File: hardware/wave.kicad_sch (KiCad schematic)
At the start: 62 parts, among them J101 WAGO 2065-100, J102 WAGO 2065-100, J103 Cortex, J104 WAGO 2065-100, J105 WAGO 2065-100, J106 WAGO 2065-100, J107 WAGO 2065-100, SW101 SKSG, SW102 SKSG, U101 ATSAMD51J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

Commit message: Refresh
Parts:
- C101, C102: Manufacturer YAGEO -> TDK; Mouser 603-CC603JRNPO9BN180 -> 810-CGA3E2C0G1H180J; Product CC0603JRNPO9BN180 -> CGA3E2C0G1H180J080AA
- INFO101: value ~ -> (none)
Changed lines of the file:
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@@
 	(title_block
 		(title "V2 wave")
-		(date "2026-02-11")
-		(rev "2026-02-11")
+		(date "2026-03-11")
+		(rev "2026-03-11")
 		(company "Versio Duo")
 		(comment 1 "Power Amplifier")
@@
 			)
 		)
-		(property "Description" "Unpolarized capacitor, small symbol"
+		(property "Description" ""
 			(at 109.22 24.13 0)
 			(effects
@@
 			)
 		)
-		(property "Description" "Push button switch, generic, two pins"
+		(property "Description" "Push button"
 			(at 256.54 30.48 0)
 			(effects
@@
 			)
 		)
-		(property "Description" "Ferrite bead, small symbol"
+		(property "Description" ""
 			(at 85.09 148.59 0)
 			(effects
@@
 			)
 		)
-		(property "Description" "Light emitting diode, small symbol"
+		(property "Description" ""
 			(at 129.54 53.34 0)
 			(effects
@@
 			)
 		)
-		(property "Description" "Resistor, small symbol"
+		(property "Description" ""
 			(at 85.09 170.18 0)
 			(effects
@@
 			)
 		)
-		(property "Description" "Resistor, small symbol"
+		(property "Description" ""
 			(at 21.59 186.69 0)
 			(effects
@@
 			)
 		)
-		(property "Description" "Unpolarized capacitor, small symbol"
+		(property "Description" ""
 			(at 199.39 45.72 0)
 			(effects
@@
 			)
 		)
-		(property "Description" "Unpolarized capacitor, small symbol"
+		(property "Description" ""
 			(at 119.38 24.13 0)
 			(effects
@@
 			)
 		)
-		(property "Description" "Resistor, small symbol"
+		(property "Description" ""
 			(at 35.56 182.88 0)
 			(effects
@@
 			)
 		)
-		(property "Value" "~"
+		(property "Value" ""
 			(at 175.895 170.815 0)
 			(effects
@@
 			)
 		)
-		(property "Description" "Unpolarized capacitor, small symbol"
+		(property "Description" ""
 			(at 173.99 45.72 0)
 			(effects
@@
 			)
 		)
-		(property "Description" "Resistor, small symbol"
+		(property "Description" ""
 			(at 21.59 179.07 0)
 			(effects
@@
 			)
 		)
-		(property "Description" "Two pin crystal, small symbol"
+		(property "Description" ""
 			(at 24.13 43.18 0)
 			(effects
@@
 			)
 		)
-		(property "Description" "Unpolarized capacitor, small symbol"
+		(property "Description" ""
 			(at 26.67 46.99 0)
 			(effects
@@
 			)
 		)
-		(property "Mouser" "603-CC603JRNPO9BN180"
+		(property "Mouser" "810-CGA3E2C0G1H180J"
 			(at 26.67 70.358 0)
 			(effects
@@
 			)
 		)
-		(property "Product" "CC0603JRNPO9BN180"
+		(property "Product" "CGA3E2C0G1H180J080AA"
 			(at 26.67 67.564 0)
 			(effects
@@
 			)
 		)
-		(property "Manufacturer" "YAGEO"
+		(property "Manufacturer" "TDK"
 			(at 26.67 64.77 0)
 			(effects
@@
 			)
 		)
-		(property "Description" "Unpolarized capacitor, small symbol"
+		(property "Description" ""
 			(at 57.15 24.13 0)
 			(effects
@@
 			)
 		)
-		(property "Description" "Unpolarized capacitor, small symbol"
+		(property "Description" ""
 			(at 21.59 46.99 0)
 			(effects
@@
 			)
 		)
-		(property "Mouser" "603-CC603JRNPO9BN180"
+		(property "Mouser" "810-CGA3E2C0G1H180J"
 			(at 21.59 70.358 0)
 			(effects
@@
 			)
 		)
-		(property "Product" "CC0603JRNPO9BN180"
+		(property "Product" "CGA3E2C0G1H180J080AA"
 			(at 21.59 67.564 0)
 			(effects
@@
 			)
 		)
-		(property "Manufacturer" "YAGEO"
+		(property "Manufacturer" "TDK"
 			(at 21.59 64.77 0)
 			(effects
@@
 			)
 		)
-		(property "Description" "Unpolarized capacitor, small symbol"
+		(property "Description" ""
 			(at 45.72 186.69 0)
 			(effects
@@
 			)
 		)
-		(property "Description" "Resistor, small symbol"
+		(property "Description" ""
 			(at 138.43 53.34 0)
 			(effects
@@
 			)
 		)
-		(property "Description" "Resistor, small symbol"
+		(property "Description" ""
 			(at 87.63 170.18 0)
 			(effects
@@
 			)
 		)
-		(property "Description" "Unpolarized capacitor, small symbol"
+		(property "Description" ""
 			(at 99.06 24.13 0)
 			(effects
@@
 			)
 		)
-		(property "Description" "Unpolarized capacitor, small symbol"
+		(property "Description" ""
 			(at 81.28 151.13 0)
 			(effects
@@
 			)
 		)
-		(property "Description" "Unpolarized capacitor, small symbol"
+		(property "Description" ""
 			(at 67.31 151.13 0)
 			(effects
@@
 			)
 		)
-		(property "Description" "Unpolarized capacitor, small symbol"
+		(property "Description" ""
 			(at 78.74 24.13 0)
 			(effects
@@
 			)
 		)
-		(property "Description" "Resistor, small symbol"
+		(property "Description" ""
 			(at 104.14 185.42 0)
 			(effects
@@
 			)
 		)
-		(property "Description" "Push button switch, generic, two pins"
+		(property "Description" "Push button"
 			(at 130.81 40.64 0)
 			(effects
@@
 			)
 		)
-		(property "Description" "Unpolarized capacitor, small symbol"
+		(property "Description" ""
 			(at 88.9 24.13 0)
 			(effects
@@
 			)
 		)
-		(property "Description" "Resistor, small symbol"
+		(property "Description" ""
 			(at 50.8 121.92 0)
 			(effects

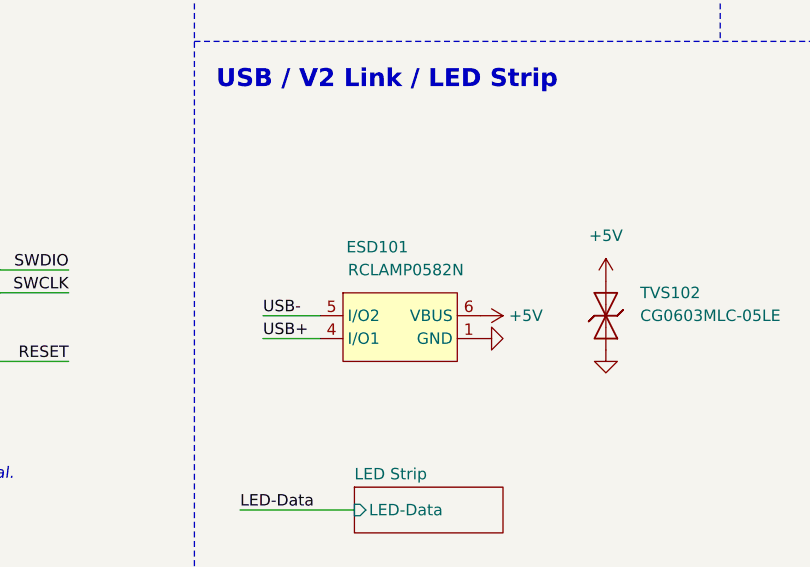
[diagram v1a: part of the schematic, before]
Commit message: Update ESD suppressor
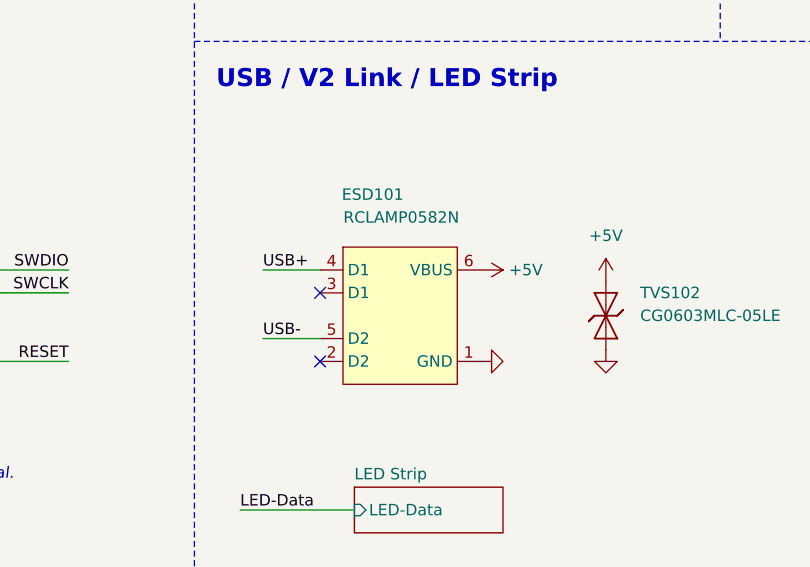
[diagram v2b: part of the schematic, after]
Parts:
- INFO101: value (none) -> ~
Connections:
- no-connect marks 27 -> 29
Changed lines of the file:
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@@
 	(title_block
 		(title "V2 wave")
-		(date "2026-03-11")
+		(date "2026-03-14")
 		(rev "2026-03-11")
 		(company "Versio Duo")
@@
 	)
 	(no_connect
+		(at 175.26 100.33)
+	)
+	(no_connect
 		(at 86.36 81.28)
 	)
@@
 	)
 	(no_connect
+		(at 175.26 107.95)
+	)
+	(no_connect
 		(at 86.36 93.98)
 	)
@@
 	(wire
 		(pts
+			(xy 168.91 97.79) (xy 175.26 97.79)
+		)
+		(stroke
+			(width 0)
+			(type default)
+		)
+	)
+	(wire
+		(pts
 			(xy 257.81 99.06) (xy 240.03 99.06)
 		)
@@
 	(wire
 		(pts
-			(xy 168.91 105.41) (xy 175.26 105.41)
-		)
-		(stroke
-			(width 0)
-			(type default)
-		)
-	)
-	(wire
-		(pts
 			(xy 256.54 46.99) (xy 271.78 46.99)
 		)
@@
 	(wire
 		(pts
-			(xy 168.91 102.87) (xy 175.26 102.87)
+			(xy 168.91 105.41) (xy 175.26 105.41)
 		)
 		(stroke
@@
 		)
 	)
+	(label "USB+"
+		(at 168.91 97.79 0)
+		(effects
+			(font
+				(size 1.27 1.27)
+			)
+			(justify left bottom)
+		)
+	)
 	(label "I2S-SCK"
 		(at 92.71 156.21 0)
@@
 	)
 	(label "USB-"
-		(at 168.91 102.87 0)
+		(at 168.91 105.41 0)
 		(effects
 			(font
@@
 		)
 	)
-	(label "USB+"
-		(at 168.91 105.41 0)
-		(effects
-			(font
-				(size 1.27 1.27)
-			)
-			(justify left bottom)
-		)
-	)
 	(label "Socket-TX"
 		(at 238.76 125.73 0)
@@
 	(symbol
 		(lib_id "V2_power:+5V")
-		(at 193.04 102.87 270)
+		(at 193.04 97.79 270)
 		(unit 1)
 		(exclude_from_sim no)
@@
 		(dnp no)
 		(property "Reference" "#PWR122"
-			(at 189.23 102.87 0)
+			(at 189.23 97.79 0)
 			(effects
 				(font
@@
 		)
 		(property "Value" "+5V"
-			(at 198.12 102.87 90)
+			(at 198.12 97.79 90)
 			(effects
 				(font
@@
 		)
 		(property "Footprint" ""
-			(at 193.04 102.87 0)
+			(at 193.04 97.79 0)
 			(effects
 				(font
@@
 		)
 		(property "Datasheet" ""
-			(at 193.04 102.87 0)
+			(at 193.04 97.79 0)
 			(effects
 				(font
@@
 		)
 		(property "Description" ""
-			(at 193.04 102.87 0)
+			(at 193.04 97.79 0)
 			(effects
 				(font
@@
 		(dnp no)
 		(property "Reference" "ESD101"
-			(at 181.61 95.25 0)
+			(at 181.102 89.408 0)
 			(effects
 				(font
@@
 		)
 		(property "Value" "RCLAMP0582N"
-			(at 184.785 97.79 0)
+			(at 184.277 91.948 0)
 			(effects
 				(font
@@
 	(symbol
 		(lib_id "V2_power:GND")
-		(at 193.04 105.41 90)
+		(at 193.04 107.95 90)
 		(unit 1)
 		(exclude_from_sim no)
@@
 		(dnp no)
 		(property "Reference" "#PWR123"
-			(at 199.39 105.41 0)
+			(at 199.39 107.95 0)
 			(effects
 				(font
@@
 		)
 		(property "Value" "GND"
-			(at 198.12 105.41 90)
+			(at 198.12 107.95 90)
 			(effects
 				(font
@@
 		)
 		(property "Footprint" ""
-			(at 193.04 105.41 0)
+			(at 193.04 107.95 0)
 			(effects
 				(font
@@
 		)
 		(property "Datasheet" ""
-			(at 193.04 105.41 0)
+			(at 193.04 107.95 0)
 			(effects
 				(font
@@
 		)
 		(property "Description" ""
-			(at 193.04 105.41 0)
+			(at 193.04 107.95 0)
 			(effects
 				(font
@@
 			)
 		)
-		(property "Value" ""
+		(property "Value" "~"
 			(at 175.895 170.815 0)
 			(effects

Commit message: Refresh
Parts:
- INFO101: value ~ -> (none)
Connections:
- net VDDCORE renamed +VDDCORE
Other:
- moved on the sheet: H105, H106

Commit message: Update
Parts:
- C101, C102, C105, C106: Id (none) -> Capacitor:${SYMBOL_NAME}; Rating (none) -> 50V
- C103, C104, C107, C108, C109, C110, C111, C112, C113: Id (none) -> Capacitor:${SYMBOL_NAME}
- D101, D102, D103: Id (none) -> LED:${SYMBOL_NAME}
- ESD101: Id (none) -> ESD:${SYMBOL_NAME}
- FB101: value 47 Ω -> 47Ω; Id (none) -> Ferrite:${SYMBOL_NAME}
- J101, J102, J104, J105, J106, J107: Id (none) -> WAGO:${SYMBOL_NAME}
- R101, R102, R103, R104, R105, R106, R107, R108: Id (none) -> Resistor:${SYMBOL_NAME}
- SW101, SW102: Id (none) -> Button:${SYMBOL_NAME}; Rating (none) -> 1.6N
- TVS101, TVS102: Id (none) -> Diode:${SYMBOL_NAME}
- U101: Id (none) -> MCU:${SYMBOL_NAME}
- U102: Id (none) -> LDO:${SYMBOL_NAME}
- Y101: Id (none) -> Crystal:${SYMBOL_NAME}

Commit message: Update
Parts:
- D101: Rating (none) -> 605nm
- D102, D103: Rating (none) -> 15mA
- ESD101: Rating (none) -> 20kV
- FB101: Rating (none) -> 5A
- J101, J102, J104, J105, J106, J107: Rating (none) -> 9A
- U101: Rating (none) -> Cortex-M4F
- U102: Rating (none) -> 300mA
- Y101: Rating (none) -> 10ppm
- renumbered C107 to C106, C106 to C107
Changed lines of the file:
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@@
 	(title_block
 		(title "V2 wave")
-		(date "2026-04-03")
-		(rev "2026-04-03")
+		(date "2026-04-14")
+		(rev "2026-04-14")
 		(company "Versio Duo")
 		(comment 1 "Power Amplifier")
@@
 		(in_pos_files yes)
 		(dnp no)
-		(property "Reference" "#PWR122"
+		(property "Reference" "#PWR123"
 			(at 189.23 97.79 0)
 			(hide yes)
@@
 			(project "wave"
 				(path "/6c8448b4-b04d-47e1-934e-e40cbe27a7be"
-					(reference "#PWR122")
+					(reference "#PWR123")
 					(unit 1)
 				)
@@
 			)
 		)
+		(property "Rating" "5A"
+			(at 100.33 148.59 0)
+			(hide yes)
+			(show_name no)
+			(do_not_autoplace no)
+			(effects
+				(font
+					(size 1.27 1.27)
+				)
+			)
+		)
 		(pin "1"
 		)
@@
 		(in_pos_files yes)
 		(dnp no)
-		(property "Reference" "#PWR110"
+		(property "Reference" "#PWR109"
 			(at 67.31 133.35 0)
 			(hide yes)
@@
 			(project "wave"
 				(path "/6c8448b4-b04d-47e1-934e-e40cbe27a7be"
-					(reference "#PWR110")
+					(reference "#PWR109")
 					(unit 1)
 				)
@@
 			)
 		)
+		(property "Rating" "300mA"
+			(at 186.69 95.25 0)
+			(hide yes)
+			(show_name no)
+			(do_not_autoplace no)
+			(effects
+				(font
+					(size 1.27 1.27)
+				)
+			)
+		)
 		(pin "1"
 		)
@@
 			)
 		)
+		(property "Rating" "605nm"
+			(at 129.54 78.74 0)
+			(hide yes)
+			(show_name no)
+			(do_not_autoplace no)
+			(effects
+				(font
+					(size 1.27 1.27)
+				)
+			)
+		)
 		(pin "1"
 		)
@@
 			)
 		)
+		(property "Rating" "15mA"
+			(at 248.92 78.74 0)
+			(hide yes)
+			(show_name no)
+			(do_not_autoplace no)
+			(effects
+				(font
+					(size 1.27 1.27)
+				)
+			)
+		)
 		(pin "1"
 		)
@@
 			)
 		)
+		(property "Rating" "20kV"
+			(at 184.15 132.08 0)
+			(hide yes)
+			(show_name no)
+			(do_not_autoplace no)
+			(effects
+				(font
+					(size 1.27 1.27)
+				)
+			)
+		)
 		(pin "1"
 		)
@@
 			)
 		)
+		(property "Rating" "9A"
+			(at 34.29 130.81 0)
+			(hide yes)
+			(show_name no)
+			(do_not_autoplace no)
+			(effects
+				(font
+					(size 1.27 1.27)
+				)
+			)
+		)
 		(pin "1"
 		)
@@
 			)
 		)
+		(property "Rating" "9A"
+			(at 135.89 181.61 0)
+			(hide yes)
+			(show_name no)
+			(do_not_autoplace no)
+			(effects
+				(font
+					(size 1.27 1.27)
+				)
+			)
+		)
 		(pin "1"
 		)
@@
 			)
 		)
+		(property "Rating" "Cortex-M4F"
+			(at 69.85 161.29 0)
+			(hide yes)
+			(show_name no)
+			(do_not_autoplace no)
+			(effects
+				(font
+					(size 1.27 1.27)
+				)
+			)
+		)
 		(pin "64"
 			(alternate "GPIOIN")
@@
 		(in_pos_files yes)
 		(dnp no)
-		(property "Reference" "#PWR123"
+		(property "Reference" "#PWR124"
 			(at 199.39 107.95 0)
 			(hide yes)
@@
 			(project "wave"
 				(path "/6c8448b4-b04d-47e1-934e-e40cbe27a7be"
-					(reference "#PWR123")
+					(reference "#PWR124")
 					(unit 1)
 				)
@@
 			)
 		)
+		(property "Rating" "15mA"
+			(at 264.16 78.74 0)
+			(hide yes)
+			(show_name no)
+			(do_not_autoplace no)
+			(effects
+				(font
+					(size 1.27 1.27)
+				)
+			)
+		)
 		(pin "1"
 		)
@@
 		(in_pos_files yes)
 		(dnp no)
-		(property "Reference" "#PWR109"
+		(property "Reference" "#PWR110"
 			(at 67.31 160.02 0)
 			(hide yes)
@@
 			(project "wave"
 				(path "/6c8448b4-b04d-47e1-934e-e40cbe27a7be"
-					(reference "#PWR109")
+					(reference "#PWR110")
 					(unit 1)
 				)
@@
 		(in_pos_files yes)
 		(dnp no)
-		(property "Reference" "#PWR113"
+		(property "Reference" "#PWR112"
 			(at 78.74 33.02 0)
 			(hide yes)
@@
 			(project "wave"
 				(path "/6c8448b4-b04d-47e1-934e-e40cbe27a7be"
-					(reference "#PWR113")
+					(reference "#PWR112")
 					(unit 1)
 				)
@@
 			)
 		)
+		(property "Rating" "10ppm"
+			(at 24.13 67.31 0)
+			(hide yes)
+			(show_name no)
+			(do_not_autoplace no)
+			(effects
+				(font
+					(size 1.27 1.27)
+				)
+			)
+		)
 		(pin "1"
 		)
@@
 			)
 		)
+		(property "Rating" "9A"
+			(at 135.89 166.37 0)
+			(hide yes)
+			(show_name no)
+			(do_not_autoplace no)
+			(effects
+				(font
+					(size 1.27 1.27)
+				)
+			)
+		)
 		(pin "1"
 		)
@@
 		(in_pos_files yes)
 		(dnp no)
-		(property "Reference" "#PWR112"
+		(property "Reference" "#PWR113"
 			(at 81.28 160.02 0)
 			(hide yes)
@@
 			(project "wave"
 				(path "/6c8448b4-b04d-47e1-934e-e40cbe27a7be"
-					(reference "#PWR112")
+					(reference "#PWR113")
 					(unit 1)
 				)
@@
 		(in_pos_files yes)
 		(dnp no)
-		(property "Reference" "#PWR124"
+		(property "Reference" "#PWR122"
 			(at 186.69 59.69 0)
 			(hide yes)
@@
 			(project "wave"
 				(path "/6c8448b4-b04d-47e1-934e-e40cbe27a7be"
-					(reference "#PWR124")
+					(reference "#PWR122")
 					(unit 1)
 				)
@@
 		(in_pos_files yes)
 		(dnp no)
-		(property "Reference" "C106"
+		(property "Reference" "C107"
 			(at 83.82 149.86 0)
 			(show_name no)
@@
 			(project "wave"
 				(path "/6c8448b4-b04d-47e1-934e-e40cbe27a7be"
-					(reference "C106")
+					(reference "C107")
 					(unit 1)
 				)
@@
 		(in_pos_files yes)
 		(dnp no)
-		(property "Reference" "C107"
+		(property "Reference" "C106"
 			(at 86.36 22.86 0)
 			(show_name no)
@@
 			(project "wave"
 				(path "/6c8448b4-b04d-47e1-934e-e40cbe27a7be"
-					(reference "C107")
+					(reference "C106")
 					(unit 1)
 				)
@@
 			)
 		)
+		(property "Rating" "9A"
+			(at 135.89 171.45 0)
+			(hide yes)
+			(show_name no)
+			(do_not_autoplace no)
+			(effects
+				(font
+					(size 1.27 1.27)
+				)
+			)
+		)
 		(pin "1"
 		)
@@
 			)
 		)
+		(property "Rating" "9A"
+			(at 135.89 176.53 0)
+			(hide yes)
+			(show_name no)
+			(do_not_autoplace no)
+			(effects
+				(font
+					(size 1.27 1.27)
+				)
+			)
+		)
 		(pin "1"
 		)
@@
 			)
 		)
+		(property "Rating" "9A"
+			(at 34.29 138.43 0)
+			(hide yes)
+			(show_name no)
+			(do_not_autoplace no)
+			(effects
+				(font
+					(size 1.27 1.27)
+				)
+			)
+		)
 		(pin "1"
 		)
@@
 			(name "V2_A4.kicad_wks")
 			(type worksheet)
-			(data |KLUv/WBhBk0QALbYTiEQtRsmZc5q276ayLS71D6kxbkmoTeIJM7lAHtEAMAAxQFGAD8ARQCbvIHa
-				a/wrVHSazXnPhvzar1BNtH1kxRf5EwCAQPh5F+e0kJq0nmtfKDvj37Jf3xQUlFKqztoXWzE7iAAI
-				iJ6Q5m2d9RAC9jcPPWe/GXf/9ewpPR3+uPbv7bdzvr37wXlr2X8dBHFXu7Z3HUG7Kvrz9qKU7eB2
-				v/MM4n/Mhfg5G5sn7WsDTS2mA1WyssZDsy4YdpEGzfD8Ny+85JzH7H+961FjX/x0qtq0MdaqJ8dx
-				k1KAwF+soV3VFnEoqewX+XNfTaqqPatRlLsbgcKhzs5+29sEzSaWRPZ4txDEjpmZNCoSiiMhaUwy
-				y4Jg3oe5pmhPRSS7MtJAerbfnYNNgaEkuCg6oVzYhbEsF1vRgtxS55zTIVig4URjFFJTI1qYFNIB
-				YESmRusYYvaiF0uSUdhu1Q2lFiOgdmN7VvaH2oWyw9MQXRuZtQQQoIsxFn2ldtnpQiUNa0HvDQCK
-				f/XTisCgEJQEXe/if4EJsakkqj8BMmGAU+ZM/AG8LSEJMfgkOKfSKPhw4rD3ZHfmNZYNfDMigEPJ
-				EBoIDghtm1kJ8BAQ8xyGdkOuFQy33sishFt8DZNX4uNRXJZ5hBy746RJaNtgbfyB613d0dov6Cdg
-				iUQT9BXkf9EiYDuODpB6gKkC|
+			(data |KLUv/WD5BbUPADbXSyEA1TbWikhSlOA2eC2ekVMEUCwq7NEwtcLUrO9RVbWigglBAD0ARQB3rDJr
+				Vfe8iEc347HKLOu3hM0n3acAgEAZ+mtWq1rqUSxebyypb/3fvvl2Ks1ai1318qyxua+IAgRM0MgT
+				vxCDqNazy01dUkv9SffBzyqWXV6zk7TDjC//75ZXzHffvHX4Y/Xf35uU+iW//OHdpP7XYKnf08G7
+				Ws+4sz/Se05W5tbSsFNFN3RTUXTjhdPWNR7ehuG4iIngvhBQHGxi+IlSiXCRzHYxEfbe576fb+gn
+				B78Z+mSX28Z5ZV5BEKwWAwQ+a06BCmH90rZJg9JtG4SrtqNsE+pn/kpSOzSUhmVScSgcO1gJcdSg
+				J6zLuq1W1TZJF+moiP3v9XDUP1+S1KFCs7SB4TTQalSg4UCjGDM0M3GaNAZgZObmWAewpQGB0gB3
+				GYWe0WuYLYxil2+HCVPCLoewmMo8a9CJow+hHPOLKHdUb0wU8lRpRE+qFdAXJgbU7nMwecZYivJQ
+				iTgLkNig5tH7xtAJA8QyZ+ZP4GUJKSTwm+RM51H7yWknvCe7YZZxrISdEQ48yLJBiQaevBZD1kY4
+				h0V7Dqlt/1rBcP0NQy83g9hYapcpANydipsbWw09qO7ggsG8qpSEBRoltBf/e9cTMh29AaQeYKo=|
 			)
-			(checksum "0A61268C685EAF945CA2EA8187370BD3")
+			(checksum "080A27BD1FADC1F81518BF82EA92C143")
 		)
 	)
